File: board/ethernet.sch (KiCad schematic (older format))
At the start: 61 parts, among them IC5 KSZ8081RNx, IC6 MAX5969x, IC7 MAX17503, J1 RJ45_LEDS, T1 749010012A, Y2 25MHz

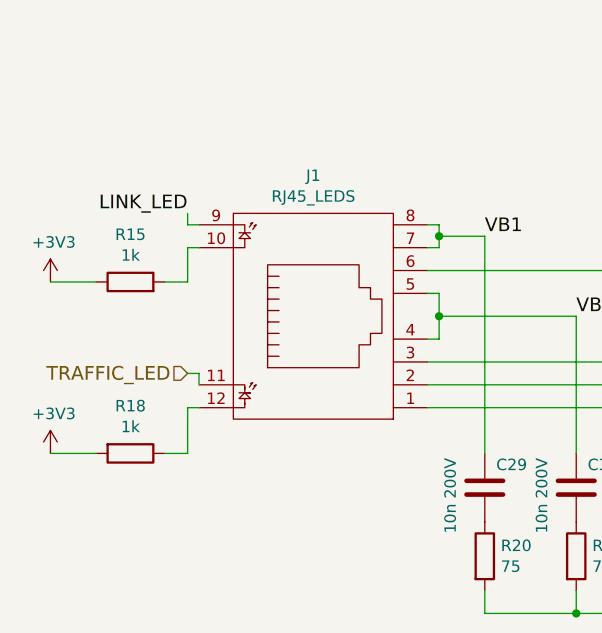
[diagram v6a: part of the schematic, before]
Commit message: Rough first go at placement minus some shrapnel
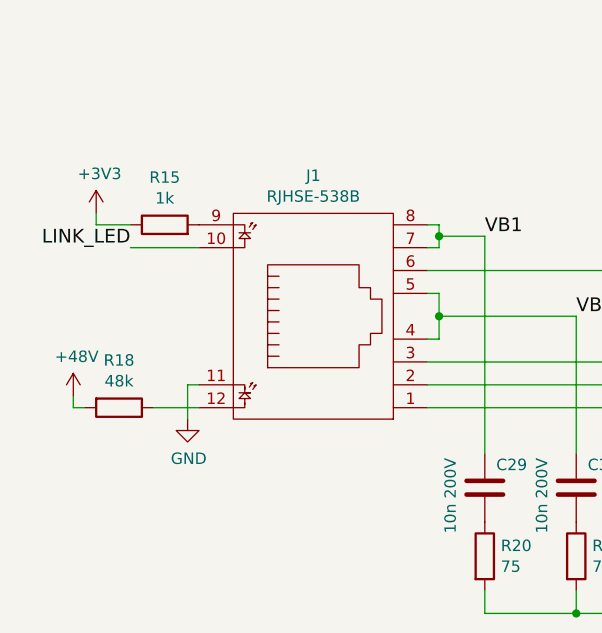
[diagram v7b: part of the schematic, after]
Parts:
- J1: value RJ45_LEDS -> RJHSE-538B; footprint Connect:RJHSE538X -> footprints:RJHSE538X; Farnell (none) -> 1860592
- R18: value 1k -> 48k
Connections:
- net TRAFFIC_LED is gone; now on net GND: J1.11
- net +3V3: no longer R18.2
- net +48V: now also R18.2
- net LINK_LED: now also J1.10; no longer J1.9
- net at R15.2: now also J1.9; no longer J1.10
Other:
- moved on the sheet: R15
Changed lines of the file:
@@
 P 2000 2250
 F 0 "J1" V 2615 2250 50  0000 C CNN
-F 1 "RJ45_LEDS" V 2524 2250 50  0000 C CNN
-F 2 "Connect:RJHSE538X" H 0   400 50  0001 C CNN
-F 3 "" H 0   400 50  0000 C CNN
+F 1 "RJHSE-538B" V 2524 2250 50  0000 C CNN
+F 2 "footprints:RJHSE538X" H 0   400 50  0001 C CNN
+F 3 "http://www.farnell.com/datasheets/1912418.pdf" H 0   400 50  0001 C CNN
+F 4 "1860592" H 2000 2250 60  0001 C CNN "Farnell"
 	1    2000 2250
 	0    -1   -1   0
@@
 	1    0    0    -1
 $EndComp
-Text HLabel 1450 2500 0    60   Input ~ 0
-TRAFFIC_LED
-$Comp
-L +3V3 #PWR51
-U 1 1 58B9F15A
-P 850 2850
-F 0 "#PWR51" H 850 2700 50  0001 C CNN
-F 1 "+3V3" H 865 3023 50  0000 C CNN
-F 2 "" H 850 2850 50  0000 C CNN
-F 3 "" H 850 2850 50  0000 C CNN
-	1    850  2850
-	1    0    0    -1
-$EndComp
-Text Label 1450 1800 2    60   ~ 0
+Text Label 1200 1950 2    60   ~ 0
 LINK_LED
 $Comp
-L +3V3 #PWR44
+L +3V3 #PWR46
 U 1 1 58B9F35C
-P 850 2100
-F 0 "#PWR44" H 850 1950 50  0001 C CNN
-F 1 "+3V3" H 865 2273 50  0000 C CNN
-F 2 "" H 850 2100 50  0000 C CNN
-F 3 "" H 850 2100 50  0000 C CNN
-	1    850  2100
+P 1050 1800
+F 0 "#PWR46" H 1050 1650 50  0001 C CNN
+F 1 "+3V3" H 1065 1973 50  0000 C CNN
+F 2 "" H 1050 1800 50  0000 C CNN
+F 3 "" H 1050 1800 50  0000 C CNN
+	1    1050 1800
 	1    0    0    -1
 $EndComp
@@
 $EndComp
 $Comp
-L GND #PWR52
+L GND #PWR55
 U 1 1 58BA0647
 P 5250 3150
-F 0 "#PWR52" H 5250 2900 50  0001 C CNN
+F 0 "#PWR55" H 5250 2900 50  0001 C CNN
 F 1 "GND" H 5255 2977 50  0000 C CNN
 F 2 "" H 5250 3150 50  0000 C CNN
@@
 $EndComp
 $Comp
-L GND #PWR53
+L GND #PWR56
 U 1 1 58BA068E
 P 5650 3150
-F 0 "#PWR53" H 5650 2900 50  0001 C CNN
+F 0 "#PWR56" H 5650 2900 50  0001 C CNN
 F 1 "GND" H 5655 2977 50  0000 C CNN
 F 2 "" H 5650 3150 50  0000 C CNN
@@
 $EndComp
 $Comp
-L GND #PWR47
+L GND #PWR49
 U 1 1 58BA115A
 P 7350 2150
-F 0 "#PWR47" H 7350 1900 50  0001 C CNN
+F 0 "#PWR49" H 7350 1900 50  0001 C CNN
 F 1 "GND" H 7355 1977 50  0001 C CNN
 F 2 "" H 7350 2150 50  0000 C CNN
@@
 $EndComp
 $Comp
-L GND #PWR55
+L GND #PWR58
 U 1 1 58BA1640
 P 6900 3500
-F 0 "#PWR55" H 6900 3250 50  0001 C CNN
+F 0 "#PWR58" H 6900 3250 50  0001 C CNN
 F 1 "GND" H 6905 3327 50  0000 C CNN
 F 2 "" H 6900 3500 50  0000 C CNN
@@
 $EndComp
 $Comp
-L GND #PWR56
+L GND #PWR59
 U 1 1 58BA1690
 P 7300 3500
-F 0 "#PWR56" H 7300 3250 50  0001 C CNN
+F 0 "#PWR59" H 7300 3250 50  0001 C CNN
 F 1 "GND" H 7305 3327 50  0000 C CNN
 F 2 "" H 7300 3500 50  0000 C CNN
@@
 $EndComp
 $Comp
-L GND #PWR45
+L GND #PWR47
 U 1 1 58BA1A5E
 P 6500 2150
-F 0 "#PWR45" H 6500 1900 50  0001 C CNN
+F 0 "#PWR47" H 6500 1900 50  0001 C CNN
 F 1 "GND" H 6505 1977 50  0001 C CNN
 F 2 "" H 6500 2150 50  0000 C CNN
@@
 $EndComp
 $Comp
-L GND #PWR46
+L GND #PWR48
 U 1 1 58BA1AB4
 P 6950 2150
-F 0 "#PWR46" H 6950 1900 50  0001 C CNN
+F 0 "#PWR48" H 6950 1900 50  0001 C CNN
 F 1 "GND" H 6955 1977 50  0001 C CNN
 F 2 "" H 6950 2150 50  0000 C CNN
@@
 $EndComp
 $Comp
-L +3V3 #PWR39
+L +3V3 #PWR41
 U 1 1 58BA1E02
 P 6050 750
-F 0 "#PWR39" H 6050 600 50  0001 C CNN
+F 0 "#PWR41" H 6050 600 50  0001 C CNN
 F 1 "+3V3" H 6065 923 50  0000 C CNN
 F 2 "" H 6050 750 50  0000 C CNN
@@
 $EndComp
 $Comp
-L GND #PWR40
+L GND #PWR42
 U 1 1 58BA48D5
 P 6450 1150
-F 0 "#PWR40" H 6450 900 50  0001 C CNN
+F 0 "#PWR42" H 6450 900 50  0001 C CNN
 F 1 "GND" H 6455 977 50  0001 C CNN
 F 2 "" H 6450 1150 50  0000 C CNN
@@
 $EndComp
 $Comp
-L GND #PWR41
+L GND #PWR43
 U 1 1 58BA492B
 P 6850 1150
-F 0 "#PWR41" H 6850 900 50  0001 C CNN
+F 0 "#PWR43" H 6850 900 50  0001 C CNN
 F 1 "GND" H 6855 977 50  0001 C CNN
 F 2 "" H 6850 1150 50  0000 C CNN
@@
 $EndComp
 $Comp
-L GND #PWR42
+L GND #PWR44
 U 1 1 58BA4B25
 P 6450 1700
-F 0 "#PWR42" H 6450 1450 50  0001 C CNN
+F 0 "#PWR44" H 6450 1450 50  0001 C CNN
 F 1 "GND" H 6455 1527 50  0001 C CNN
 F 2 "" H 6450 1700 50  0000 C CNN
@@
 $EndComp
 $Comp
-L GND #PWR43
+L GND #PWR45
 U 1 1 58BA4BE5
 P 6850 1700
-F 0 "#PWR43" H 6850 1450 50  0001 C CNN
+F 0 "#PWR45" H 6850 1450 50  0001 C CNN
 F 1 "GND" H 6855 1527 50  0001 C CNN
 F 2 "" H 6850 1700 50  0000 C CNN
@@
 $EndComp
 $Comp
-L +3V3 #PWR48
+L +3V3 #PWR50
 U 1 1 58BA8C0B
 P 9550 2150
-F 0 "#PWR48" H 9550 2000 50  0001 C CNN
+F 0 "#PWR50" H 9550 2000 50  0001 C CNN
 F 1 "+3V3" H 9565 2323 50  0000 C CNN
 F 2 "" H 9550 2150 50  0000 C CNN
@@
 $EndComp
 $Comp
-L GND #PWR50
+L GND #PWR54
 U 1 1 58BABD3E
 P 9700 2800
-F 0 "#PWR50" H 9700 2550 50  0001 C CNN
+F 0 "#PWR54" H 9700 2550 50  0001 C CNN
 F 1 "GND" H 9705 2627 50  0000 C CNN
 F 2 "" H 9700 2800 50  0000 C CNN
@@
 $EndComp
 $Comp
-L +3V3 #PWR49
+L +3V3 #PWR52
 U 1 1 58BAD620
 P 10200 2600
-F 0 "#PWR49" H 10200 2450 50  0001 C CNN
+F 0 "#PWR52" H 10200 2450 50  0001 C CNN
 F 1 "+3V3" H 10215 2773 50  0000 C CNN
 F 2 "" H 10200 2600 50  0000 C CNN
@@
 $EndComp
 $Comp
-L GND #PWR54
+L GND #PWR57
 U 1 1 58BAD7C0
 P 10200 3350
-F 0 "#PWR54" H 10200 3100 50  0001 C CNN
+F 0 "#PWR57" H 10200 3100 50  0001 C CNN
 F 1 "GND" H 10205 3177 50  0000 C CNN
 F 2 "" H 10200 3350 50  0000 C CNN
@@
 L R R15
 U 1 1 58BB03BC
-P 1200 2100
-F 0 "R15" V 1407 2100 50  0000 C CNN
-F 1 "1k" V 1316 2100 50  0000 C CNN
-F 2 "agg:0603" V 1130 2100 50  0001 C CNN
-F 3 "" H 1200 2100 50  0000 C CNN
-	1    1200 2100
+P 1350 1850
+F 0 "R15" V 1557 1850 50  0000 C CNN
+F 1 "1k" V 1466 1850 50  0000 C CNN
+F 2 "agg:0603" V 1280 1850 50  0001 C CNN
+F 3 "" H 1350 1850 50  0000 C CNN
+	1    1350 1850
 	0    -1   -1   0
-$EndComp
-$Comp
-L R R18
-U 1 1 58BB1419
-P 1200 2850
-F 0 "R18" V 993 2850 50  0000 C CNN
-F 1 "1k" V 1084 2850 50  0000 C CNN
-F 2 "agg:0603" V 1130 2850 50  0001 C CNN
-F 3 "" H 1200 2850 50  0000 C CNN
-	1    1200 2850
-	0    1    1    0
 $EndComp
 $Comp
@@
 NoConn ~ 4700 4700
 $Comp
-L GND #PWR61
+L GND #PWR64
 U 1 1 58BC4A36
 P 4800 5300
-F 0 "#PWR61" H 4800 5050 50  0001 C CNN
+F 0 "#PWR64" H 4800 5050 50  0001 C CNN
 F 1 "GND" H 4805 5127 50  0000 C CNN
 F 2 "" H 4800 5300 50  0000 C CNN
@@
 $EndComp
 $Comp
-L GND #PWR57
+L GND #PWR60
 U 1 1 58BC73C0
 P 6400 4600
-F 0 "#PWR57" H 6400 4350 50  0001 C CNN
+F 0 "#PWR60" H 6400 4350 50  0001 C CNN
 F 1 "GND" H 6405 4427 50  0000 C CNN
 F 2 "" H 6400 4600 50  0000 C CNN
@@
 NoConn ~ 6750 5100
 $Comp
-L GND #PWR60
+L GND #PWR63
 U 1 1 58BC9E72
 P 6700 5200
-F 0 "#PWR60" H 6700 4950 50  0001 C CNN
+F 0 "#PWR63" H 6700 4950 50  0001 C CNN
 F 1 "GND" H 6705 5027 50  0001 C CNN
 F 2 "" H 6700 5200 50  0000 C CNN
@@
 $EndComp
 $Comp
-L GND #PWR63
+L GND #PWR66
 U 1 1 58BCA458
 P 6200 5700
-F 0 "#PWR63" H 6200 5450 50  0001 C CNN
+F 0 "#PWR66" H 6200 5450 50  0001 C CNN
 F 1 "GND" H 6205 5527 50  0000 C CNN
 F 2 "" H 6200 5700 50  0000 C CNN
@@
 NoConn ~ 6750 5500
 $Comp
-L GND #PWR64
+L GND #PWR67
 U 1 1 58BCAA6F
 P 6650 6050
-F 0 "#PWR64" H 6650 5800 50  0001 C CNN
+F 0 "#PWR67" H 6650 5800 50  0001 C CNN
 F 1 "GND" H 6655 5877 50  0000 C CNN
 F 2 "" H 6650 6050 50  0000 C CNN
@@
 NoConn ~ 7750 5600
 $Comp
-L GND #PWR66
+L GND #PWR69
 U 1 1 58BCCF2C
 P 7950 6100
-F 0 "#PWR66" H 7950 5850 50  0001 C CNN
+F 0 "#PWR69" H 7950 5850 50  0001 C CNN
 F 1 "GND" H 7955 5927 50  0000 C CNN
 F 2 "" H 7950 6100 50  0000 C CNN
@@
 $EndComp
 $Comp
-L GND #PWR67
+L GND #PWR70
 U 1 1 58BCD1A4
 P 8250 6100
-F 0 "#PWR67" H 8250 5850 50  0001 C CNN
+F 0 "#PWR70" H 8250 5850 50  0001 C CNN
 F 1 "GND" H 8255 5927 50  0000 C CNN
 F 2 "" H 8250 6100 50  0000 C CNN
@@
 $EndComp
 $Comp
-L GND #PWR62
+L GND #PWR65
 U 1 1 58BCDD4D
 P 8900 5350
-F 0 "#PWR62" H 8900 5100 50  0001 C CNN
+F 0 "#PWR65" H 8900 5100 50  0001 C CNN
 F 1 "GND" H 8905 5177 50  0000 C CNN
 F 2 "" H 8900 5350 50  0000 C CNN
@@
 $EndComp
 $Comp
-L GND #PWR65
+L GND #PWR68
 U 1 1 58BCE5C3
 P 9350 6050
-F 0 "#PWR65" H 9350 5800 50  0001 C CNN
+F 0 "#PWR68" H 9350 5800 50  0001 C CNN
 F 1 "GND" H 9355 5877 50  0000 C CNN
 F 2 "" H 9350 6050 50  0000 C CNN
@@
 $EndComp
 $Comp
-L +12V #PWR59
+L +12V #PWR62
 U 1 1 58BCF882
 P 9800 5000
-F 0 "#PWR59" H 9800 4850 50  0001 C CNN
+F 0 "#PWR62" H 9800 4850 50  0001 C CNN
 F 1 "+12V" V 9815 5128 50  0000 L CNN
 F 2 "" H 9800 5000 50  0000 C CNN
@@
 +48V
 Wire Wire Line
-	1450 2850 1450 2650
-Wire Wire Line
-	1450 2650 1500 2650
-Wire Wire Line
-	1450 2100 1450 1950
-Wire Wire Line
-	1450 1950 1500 1950
+	1200 1950 1500 1950
 Wire Wire Line
 	2550 1900 2750 1900
@@
 	10200 2600 10200 2650
 Connection ~ 10200 2650
-Wire Wire Line
-	1450 1800 1450 1850
-Wire Wire Line
-	1450 1850 1500 1850
-Wire Wire Line
-	1350 2100 1450 2100
-Wire Wire Line
-	1050 2100 850  2100
-Wire Wire Line
-	1450 2500 1500 2500
-Wire Wire Line
-	1500 2500 1500 2550
-Wire Wire Line
-	850  2850 1050 2850
-Wire Wire Line
-	1350 2850 1450 2850
 Wire Wire Line
 	1150 5050 1200 5050
@@
 	9350 5650 8600 5650
 $Comp
-L +12V #PWR58
+L +12V #PWR61
 U 1 1 58BC71BD
 P 4900 4700
-F 0 "#PWR58" H 4900 4550 50  0001 C CNN
+F 0 "#PWR61" H 4900 4550 50  0001 C CNN
 F 1 "+12V" H 4915 4873 50  0000 C CNN
 F 2 "" H 4900 4700 50  0000 C CNN
@@
 	5200 5100 5200 5000
 Connection ~ 5200 5000
+$Comp
+L +48V #PWR51
+U 1 1 58DB5468
+P 950 2600
+F 0 "#PWR51" H 950 2450 50  0001 C CNN
+F 1 "+48V" H 965 2773 50  0000 C CNN
+F 2 "" H 950 2600 50  0001 C CNN
+F 3 "" H 950 2600 50  0001 C CNN
+	1    950  2600
+	1    0    0    -1
+$EndComp
+$Comp
+L R R18
+U 1 1 58DB5701
+P 1150 2650
+F 0 "R18" V 943 2650 50  0000 C CNN
+F 1 "48k" V 1034 2650 50  0000 C CNN
+F 2 "agg:0603" V 1080 2650 50  0001 C CNN
+F 3 "" H 1150 2650 50  0001 C CNN
+	1    1150 2650
+	0    1    1    0
+$EndComp
+$Comp
+L GND #PWR53
+U 1 1 58DB5B5A
+P 1450 2700
+F 0 "#PWR53" H 1450 2450 50  0001 C CNN
+F 1 "GND" H 1455 2527 50  0000 C CNN
+F 2 "" H 1450 2700 50  0001 C CNN
+F 3 "" H 1450 2700 50  0001 C CNN
+	1    1450 2700
+	1    0    0    -1
+$EndComp
+Wire Wire Line
+	950  2600 950  2650
+Wire Wire Line
+	950  2650 1000 2650
+Wire Wire Line
+	1300 2650 1500 2650
+Wire Wire Line
+	1500 2550 1450 2550
+Wire Wire Line
+	1450 2550 1450 2700
+Wire Wire Line
+	1050 1800 1050 1850
+Wire Wire Line
+	1050 1850 1200 1850
 $EndSCHEMATC
